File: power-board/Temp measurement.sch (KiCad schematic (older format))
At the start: 8 parts, among them U5 AT30TS74-XM

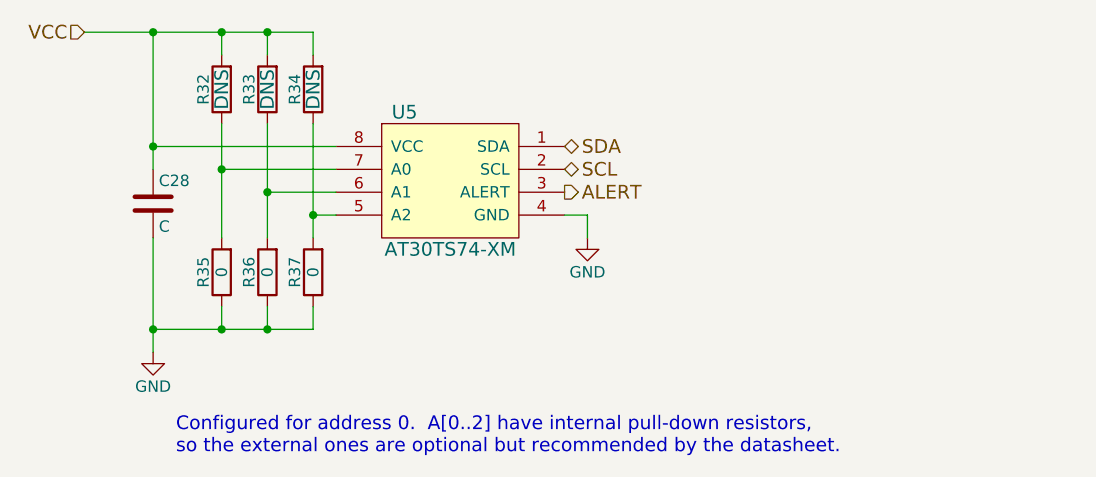
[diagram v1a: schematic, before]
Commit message: switched to XMEGA A4U
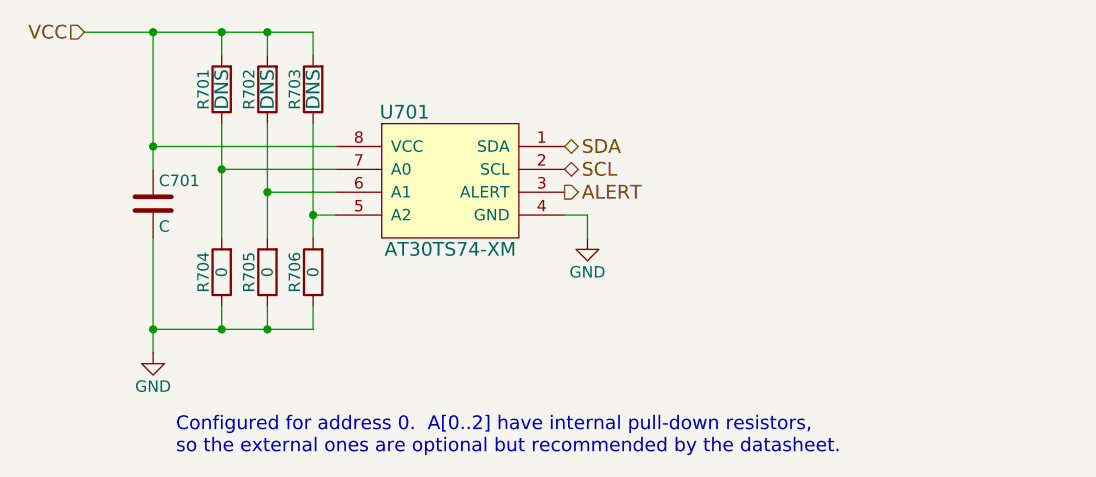
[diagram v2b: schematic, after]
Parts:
- renumbered C28 to C701, R32 to R701, R33 to R702, R34 to R703, R35 to R704, R36 to R705, R37 to R706, U5 to U701
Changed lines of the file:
@@
 $Descr A4 11693 8268
 encoding utf-8
-Sheet 7 10
+Sheet 7 11
 Title ""
 Date ""
@@
 $EndDescr
 $Comp
-L AT30TS74-XM U5
+L AT30TS74-XM U701
 U 1 1 59359173
 P 5500 3650
-F 0 "U5" H 5600 3700 60  0000 C CNN
+F 0 "U701" H 5600 3700 60  0000 C CNN
 F 1 "AT30TS74-XM" H 5800 3100 60  0000 C CNN
 F 2 "" H 5500 3650 60  0000 C CNN
@@
 ALERT
 $Comp
-L GND #PWR34
+L GND #PWR042
 U 1 1 5935935B
 P 6400 4150
-F 0 "#PWR34" H 6400 3900 50  0001 C CNN
+F 0 "#PWR042" H 6400 3900 50  0001 C CNN
 F 1 "GND" H 6400 4000 50  0000 C CNN
 F 2 "" H 6400 4150 50  0000 C CNN
@@
 	6400 4050 6400 4150
 $Comp
-L C C28
+L C C701
 U 1 1 59359380
 P 4500 4000
-F 0 "C28" H 4525 4100 50  0000 L CNN
+F 0 "C701" H 4525 4100 50  0000 L CNN
 F 1 "C" H 4525 3900 50  0000 L CNN
 F 2 "" H 4538 3850 50  0000 C CNN
@@
 $EndComp
 $Comp
-L R R37
+L R R706
 U 1 1 593595A6
 P 5200 4300
-F 0 "R37" V 5280 4300 50  0000 C CNN
+F 0 "R706" V 5280 4300 50  0000 C CNN
 F 1 "0" V 5200 4300 50  0000 C CNN
 F 2 "" V 5130 4300 50  0000 C CNN
@@
 $EndComp
 $Comp
-L R R36
+L R R705
 U 1 1 59359612
 P 5000 4300
-F 0 "R36" V 5080 4300 50  0000 C CNN
+F 0 "R705" V 5080 4300 50  0000 C CNN
 F 1 "0" V 5000 4300 50  0000 C CNN
 F 2 "" V 4930 4300 50  0000 C CNN
@@
 $EndComp
 $Comp
-L R R35
+L R R704
 U 1 1 59359639
 P 4800 4300
-F 0 "R35" V 4880 4300 50  0000 C CNN
+F 0 "R704" V 4880 4300 50  0000 C CNN
 F 1 "0" V 4800 4300 50  0000 C CNN
 F 2 "" V 4730 4300 50  0000 C CNN
@@
 $EndComp
 $Comp
-L R R32
+L R R701
 U 1 1 593597EF
 P 4800 3500
-F 0 "R32" V 4880 3500 50  0000 C CNN
+F 0 "R701" V 4880 3500 50  0000 C CNN
 F 1 "R" V 4800 3500 50  0001 C CNN
 F 2 "" V 4730 3500 50  0000 C CNN
@@
 	5000 4550 5000 4450
 $Comp
-L GND #PWR35
+L GND #PWR043
 U 1 1 59359C4C
 P 4500 4650
-F 0 "#PWR35" H 4500 4400 50  0001 C CNN
+F 0 "#PWR043" H 4500 4400 50  0001 C CNN
 F 1 "GND" H 4500 4500 50  0000 C CNN
 F 2 "" H 4500 4650 50  0000 C CNN
@@
 $EndComp
 $Comp
-L R R33
+L R R702
 U 1 1 59359E6E
 P 5000 3500
-F 0 "R33" V 5080 3500 50  0000 C CNN
+F 0 "R702" V 5080 3500 50  0000 C CNN
 F 1 "R" V 5000 3500 50  0001 C CNN
 F 2 "" V 4930 3500 50  0000 C CNN
@@
 $EndComp
 $Comp
-L R R34
+L R R703
 U 1 1 59359E9C
 P 5200 3500
-F 0 "R34" V 5280 3500 50  0000 C CNN
+F 0 "R703" V 5280 3500 50  0000 C CNN
 F 1 "R" V 5200 3500 50  0001 C CNN
 F 2 "" V 5130 3500 50  0000 C CNN

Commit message: routed board
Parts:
- C701: value C -> 0.1u; footprint (none) -> Capacitors_SMD:C_0603
- R701, R702, R703, R704, R705, R706: footprint (none) -> Resistors_SMD:R_0603
- U701: value AT30TS74-XM -> Main Reg; footprint (none) -> Housings_SSOP:MSOP-8_3x3mm_Pitch0.65mm
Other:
- moved on the sheet: R701, R702, R703, R704, R705, R706, U701
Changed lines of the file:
@@
 $Descr A4 11693 8268
 encoding utf-8
-Sheet 7 11
+Sheet 6 12
 Title ""
 Date ""
@@
 L AT30TS74-XM U701
 U 1 1 59359173
-P 5500 3650
-F 0 "U701" H 5600 3700 60  0000 C CNN
-F 1 "AT30TS74-XM" H 5800 3100 60  0000 C CNN
-F 2 "" H 5500 3650 60  0000 C CNN
-F 3 "" H 5500 3650 60  0000 C CNN
-F 4 "Microchip Technology" H 5500 3650 60  0001 C CNN "MFG"
-F 5 "AT30TS74-XM8M-B" H 5500 3650 60  0001 C CNN "MPN"
-	1    5500 3650
+P 6300 3700
+F 0 "U701" H 6400 3750 60  0000 C CNN
+F 1 "Main Reg" H 6600 3150 60  0000 C CNN
+F 2 "Housings_SSOP:MSOP-8_3x3mm_Pitch0.65mm" H 6300 3700 60  0001 C CNN
+F 3 "" H 6300 3700 60  0000 C CNN
+F 4 "Microchip Technology" H 6300 3700 60  0001 C CNN "MFG"
+F 5 "AT30TS74-XM8M-B" H 6300 3700 60  0001 C CNN "MPN"
+	1    6300 3700
 	1    0    0    -1
 $EndComp
-Text HLabel 4200 3250 0    60   Input ~ 0
+Text HLabel 5000 3300 0    60   Input ~ 0
 VCC
-Text HLabel 6300 3750 2    60   BiDi ~ 0
+Text HLabel 7100 3800 2    60   BiDi ~ 0
 SDA
-Text HLabel 6300 3850 2    60   BiDi ~ 0
+Text HLabel 7100 3900 2    60   BiDi ~ 0
 SCL
-Text HLabel 6300 3950 2    60   Output ~ 0
+Text HLabel 7100 4000 2    60   Output ~ 0
 ALERT
 $Comp
-L GND #PWR042
+L GND #PWR028
 U 1 1 5935935B
-P 6400 4150
-F 0 "#PWR042" H 6400 3900 50  0001 C CNN
-F 1 "GND" H 6400 4000 50  0000 C CNN
-F 2 "" H 6400 4150 50  0000 C CNN
-F 3 "" H 6400 4150 50  0000 C CNN
-	1    6400 4150
+P 7200 4200
+F 0 "#PWR028" H 7200 3950 50  0001 C CNN
+F 1 "GND" H 7200 4050 50  0000 C CNN
+F 2 "" H 7200 4200 50  0000 C CNN
+F 3 "" H 7200 4200 50  0000 C CNN
+	1    7200 4200
 	1    0    0    -1
 $EndComp
 Wire Wire Line
-	6300 4050 6400 4050
+	7100 4100 7200 4100
 Wire Wire Line
-	6400 4050 6400 4150
-$Comp
-L C C701
-U 1 1 59359380
-P 4500 4000
-F 0 "C701" H 4525 4100 50  0000 L CNN
-F 1 "C" H 4525 3900 50  0000 L CNN
-F 2 "" H 4538 3850 50  0000 C CNN
-F 3 "" H 4500 4000 50  0000 C CNN
-F 4 "Murata Electronics" H 4500 4000 60  0001 C CNN "MFG"
-F 5 "GRM188R71H104KA93D" H 4500 4000 60  0001 C CNN "MPN"
-	1    4500 4000
-	1    0    0    -1
-$EndComp
+	7200 4100 7200 4200
 $Comp
 L R R706
 U 1 1 593595A6
-P 5200 4300
-F 0 "R706" V 5280 4300 50  0000 C CNN
-F 1 "0" V 5200 4300 50  0000 C CNN
-F 2 "" V 5130 4300 50  0000 C CNN
-F 3 "" H 5200 4300 50  0000 C CNN
-	1    5200 4300
+P 6000 4350
+F 0 "R706" V 6080 4350 50  0000 C CNN
+F 1 "0" V 6000 4350 50  0000 C CNN
+F 2 "Resistors_SMD:R_0603" V 5930 4350 50  0001 C CNN
+F 3 "" H 6000 4350 50  0000 C CNN
+	1    6000 4350
 	-1   0    0    1
 $EndComp
@@
 L R R705
 U 1 1 59359612
-P 5000 4300
-F 0 "R705" V 5080 4300 50  0000 C CNN
-F 1 "0" V 5000 4300 50  0000 C CNN
-F 2 "" V 4930 4300 50  0000 C CNN
-F 3 "" H 5000 4300 50  0000 C CNN
-	1    5000 4300
+P 5800 4350
+F 0 "R705" V 5880 4350 50  0000 C CNN
+F 1 "0" V 5800 4350 50  0000 C CNN
+F 2 "Resistors_SMD:R_0603" V 5730 4350 50  0001 C CNN
+F 3 "" H 5800 4350 50  0000 C CNN
+	1    5800 4350
 	-1   0    0    1
 $EndComp
@@
 L R R704
 U 1 1 59359639
-P 4800 4300
-F 0 "R704" V 4880 4300 50  0000 C CNN
-F 1 "0" V 4800 4300 50  0000 C CNN
-F 2 "" V 4730 4300 50  0000 C CNN
-F 3 "" H 4800 4300 50  0000 C CNN
-	1    4800 4300
+P 5600 4350
+F 0 "R704" V 5680 4350 50  0000 C CNN
+F 1 "0" V 5600 4350 50  0000 C CNN
+F 2 "Resistors_SMD:R_0603" V 5530 4350 50  0001 C CNN
+F 3 "" H 5600 4350 50  0000 C CNN
+	1    5600 4350
 	-1   0    0    1
 $EndComp
@@
 L R R701
 U 1 1 593597EF
-P 4800 3500
-F 0 "R701" V 4880 3500 50  0000 C CNN
-F 1 "R" V 4800 3500 50  0001 C CNN
-F 2 "" V 4730 3500 50  0000 C CNN
-F 3 "" H 4800 3500 50  0000 C CNN
-F 4 "DNS" V 4800 3500 60  0000 C CNN "Note"
-	1    4800 3500
+P 5600 3550
+F 0 "R701" V 5680 3550 50  0000 C CNN
+F 1 "R" V 5600 3550 50  0001 C CNN
+F 2 "Resistors_SMD:R_0603" V 5530 3550 50  0001 C CNN
+F 3 "" H 5600 3550 50  0000 C CNN
+F 4 "DNS" V 5600 3550 60  0000 C CNN "Note"
+	1    5600 3550
 	-1   0    0    1
 $EndComp
 Wire Wire Line
-	5300 3850 4800 3850
+	6100 3900 5600 3900
 Wire Wire Line
-	4800 3650 4800 4150
-Connection ~ 4800 3850
+	5600 3700 5600 4200
+Connection ~ 5600 3900
 Wire Wire Line
-	5300 3950 5000 3950
+	6100 4000 5800 4000
 Wire Wire Line
-	5000 3650 5000 4150
-Connection ~ 5000 3950
+	5800 3700 5800 4200
+Connection ~ 5800 4000
 Wire Wire Line
-	5300 4050 5200 4050
+	6100 4100 6000 4100
 Wire Wire Line
-	5200 3650 5200 4150
-Connection ~ 5200 4050
+	6000 3700 6000 4200
+Connection ~ 6000 4100
 Wire Wire Line
-	5200 4550 5200 4450
+	6000 4600 6000 4500
 Wire Wire Line
-	4500 4550 5200 4550
+	5300 4600 6000 4600
 Wire Wire Line
-	4800 4550 4800 4450
-Connection ~ 5000 4550
+	5600 4600 5600 4500
+Connection ~ 5800 4600
 Wire Wire Line
-	4800 3250 4800 3350
+	5600 3300 5600 3400
 Wire Wire Line
-	4200 3250 5200 3250
+	5000 3300 6000 3300
 Wire Wire Line
-	5200 3250 5200 3350
+	6000 3300 6000 3400
 Wire Wire Line
-	5000 3350 5000 3250
-Connection ~ 5000 3250
-Connection ~ 4800 3250
+	5800 3400 5800 3300
+Connection ~ 5800 3300
+Connection ~ 5600 3300
 Wire Wire Line
-	5300 3750 4500 3750
+	6100 3800 5300 3800
 Wire Wire Line
-	4500 3250 4500 3850
-Connection ~ 4500 3250
-Connection ~ 4500 3750
+	5300 3300 5300 3900
+Connection ~ 5300 3300
+Connection ~ 5300 3800
 Wire Wire Line
-	4500 4150 4500 4650
-Connection ~ 4800 4550
-Connection ~ 4500 4550
+	5300 4200 5300 4700
+Connection ~ 5600 4600
+Connection ~ 5300 4600
 Wire Wire Line
-	5000 4550 5000 4450
+	5800 4600 5800 4500
 $Comp
-L GND #PWR043
+L GND #PWR029
 U 1 1 59359C4C
-P 4500 4650
-F 0 "#PWR043" H 4500 4400 50  0001 C CNN
-F 1 "GND" H 4500 4500 50  0000 C CNN
-F 2 "" H 4500 4650 50  0000 C CNN
-F 3 "" H 4500 4650 50  0000 C CNN
-	1    4500 4650
+P 5300 4700
+F 0 "#PWR029" H 5300 4450 50  0001 C CNN
+F 1 "GND" H 5300 4550 50  0000 C CNN
+F 2 "" H 5300 4700 50  0000 C CNN
+F 3 "" H 5300 4700 50  0000 C CNN
+	1    5300 4700
 	1    0    0    -1
 $EndComp
@@
 L R R702
 U 1 1 59359E6E
-P 5000 3500
-F 0 "R702" V 5080 3500 50  0000 C CNN
-F 1 "R" V 5000 3500 50  0001 C CNN
-F 2 "" V 4930 3500 50  0000 C CNN
-F 3 "" H 5000 3500 50  0000 C CNN
-F 4 "DNS" V 5000 3500 60  0000 C CNN "Note"
-	1    5000 3500
+P 5800 3550
+F 0 "R702" V 5880 3550 50  0000 C CNN
+F 1 "R" V 5800 3550 50  0001 C CNN
+F 2 "Resistors_SMD:R_0603" V 5730 3550 50  0001 C CNN
+F 3 "" H 5800 3550 50  0000 C CNN
+F 4 "DNS" V 5800 3550 60  0000 C CNN "Note"
+	1    5800 3550
 	-1   0    0    1
 $EndComp
@@
 L R R703
 U 1 1 59359E9C
-P 5200 3500
-F 0 "R703" V 5280 3500 50  0000 C CNN
-F 1 "R" V 5200 3500 50  0001 C CNN
-F 2 "" V 5130 3500 50  0000 C CNN
-F 3 "" H 5200 3500 50  0000 C CNN
-F 4 "DNS" V 5200 3500 60  0000 C CNN "Note"
-	1    5200 3500
+P 6000 3550
+F 0 "R703" V 6080 3550 50  0000 C CNN
+F 1 "R" V 6000 3550 50  0001 C CNN
+F 2 "Resistors_SMD:R_0603" V 5930 3550 50  0001 C CNN
+F 3 "" H 6000 3550 50  0000 C CNN
+F 4 "DNS" V 6000 3550 60  0000 C CNN "Note"
+	1    6000 3550
 	-1   0    0    1
 $EndComp
 Text Notes 4600 5100 0    60   ~ 0
 Configured for address 0.  A[0..2] have internal pull-down resistors,\nso the external ones are optional but recommended by the datasheet.
+$Comp
+L C C701
+U 1 1 593E171E
+P 5300 4050
+F 0 "C701" H 5325 4150 50  0000 L CNN
+F 1 "0.1u" H 5325 3950 50  0000 L CNN
+F 2 "Capacitors_SMD:C_0603" H 5338 3900 50  0001 C CNN
+F 3 "" H 5300 4050 50  0000 C CNN
+F 4 "Murata Electronics" H 5300 4050 60  0001 C CNN "MFG"
+F 5 "GRM188R71H104KA93D" H 5300 4050 60  0001 C CNN "MPN"
+	1    5300 4050
+	1    0    0    -1
+$EndComp
 $EndSCHEMATC

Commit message: adding more part numbers
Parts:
- R701, R702, R703, R704, R705, R706: MFG (none) -> Yageo; MPN (none) -> RC0603JR-070RL
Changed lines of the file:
@@
 	7200 4100 7200 4200
-$Comp
-L R R706
-U 1 1 593595A6
-P 6000 4350
-F 0 "R706" V 6080 4350 50  0000 C CNN
-F 1 "0" V 6000 4350 50  0000 C CNN
-F 2 "Resistors_SMD:R_0603" V 5930 4350 50  0001 C CNN
-F 3 "" H 6000 4350 50  0000 C CNN
-	1    6000 4350
-	-1   0    0    1
-$EndComp
-$Comp
-L R R705
-U 1 1 59359612
-P 5800 4350
-F 0 "R705" V 5880 4350 50  0000 C CNN
-F 1 "0" V 5800 4350 50  0000 C CNN
-F 2 "Resistors_SMD:R_0603" V 5730 4350 50  0001 C CNN
-F 3 "" H 5800 4350 50  0000 C CNN
-	1    5800 4350
-	-1   0    0    1
-$EndComp
 $Comp
 L R R704
@@
 F 2 "Resistors_SMD:R_0603" V 5530 4350 50  0001 C CNN
 F 3 "" H 5600 4350 50  0000 C CNN
+F 4 "Yageo" V 5600 4350 60  0001 C CNN "MFG"
+F 5 "RC0603JR-070RL" V 5600 4350 60  0001 C CNN "MPN"
 	1    5600 4350
 	-1   0    0    1
@@
 F 3 "" H 5600 3550 50  0000 C CNN
 F 4 "DNS" V 5600 3550 60  0000 C CNN "Note"
+F 5 "Yageo" V 5600 3550 60  0001 C CNN "MFG"
+F 6 "RC0603JR-070RL" V 5600 3550 60  0001 C CNN "MPN"
 	1    5600 3550
 	-1   0    0    1
@@
 	1    0    0    -1
 $EndComp
-$Comp
-L R R702
-U 1 1 59359E6E
-P 5800 3550
-F 0 "R702" V 5880 3550 50  0000 C CNN
-F 1 "R" V 5800 3550 50  0001 C CNN
-F 2 "Resistors_SMD:R_0603" V 5730 3550 50  0001 C CNN
-F 3 "" H 5800 3550 50  0000 C CNN
-F 4 "DNS" V 5800 3550 60  0000 C CNN "Note"
-	1    5800 3550
-	-1   0    0    1
-$EndComp
-$Comp
-L R R703
-U 1 1 59359E9C
-P 6000 3550
-F 0 "R703" V 6080 3550 50  0000 C CNN
-F 1 "R" V 6000 3550 50  0001 C CNN
-F 2 "Resistors_SMD:R_0603" V 5930 3550 50  0001 C CNN
-F 3 "" H 6000 3550 50  0000 C CNN
-F 4 "DNS" V 6000 3550 60  0000 C CNN "Note"
-	1    6000 3550
-	-1   0    0    1
-$EndComp
 Text Notes 4600 5100 0    60   ~ 0
 Configured for address 0.  A[0..2] have internal pull-down resistors,\nso the external ones are optional but recommended by the datasheet.
@@
 	1    0    0    -1
 $EndComp
+$Comp
+L R R705
+U 1 1 59AB8DA0
+P 5800 4350
+F 0 "R705" V 5880 4350 50  0000 C CNN
+F 1 "0" V 5800 4350 50  0000 C CNN
+F 2 "Resistors_SMD:R_0603" V 5730 4350 50  0001 C CNN
+F 3 "" H 5800 4350 50  0000 C CNN
+F 4 "Yageo" V 5800 4350 60  0001 C CNN "MFG"
+F 5 "RC0603JR-070RL" V 5800 4350 60  0001 C CNN "MPN"
+	1    5800 4350
+	-1   0    0    1
+$EndComp
+$Comp
+L R R706
+U 1 1 59AB8DCD
+P 6000 4350
+F 0 "R706" V 6080 4350 50  0000 C CNN
+F 1 "0" V 6000 4350 50  0000 C CNN
+F 2 "Resistors_SMD:R_0603" V 5930 4350 50  0001 C CNN
+F 3 "" H 6000 4350 50  0000 C CNN
+F 4 "Yageo" V 6000 4350 60  0001 C CNN "MFG"
+F 5 "RC0603JR-070RL" V 6000 4350 60  0001 C CNN "MPN"
+	1    6000 4350
+	-1   0    0    1
+$EndComp
+$Comp
+L R R702
+U 1 1 59ABAD46
+P 5800 3550
+F 0 "R702" V 5880 3550 50  0000 C CNN
+F 1 "R" V 5800 3550 50  0001 C CNN
+F 2 "Resistors_SMD:R_0603" V 5730 3550 50  0001 C CNN
+F 3 "" H 5800 3550 50  0000 C CNN
+F 4 "DNS" V 5800 3550 60  0000 C CNN "Note"
+F 5 "Yageo" V 5800 3550 60  0001 C CNN "MFG"
+F 6 "RC0603JR-070RL" V 5800 3550 60  0001 C CNN "MPN"
+	1    5800 3550
+	-1   0    0    1
+$EndComp
+$Comp
+L R R703
+U 1 1 59ABAD73
+P 6000 3550
+F 0 "R703" V 6080 3550 50  0000 C CNN
+F 1 "R" V 6000 3550 50  0001 C CNN
+F 2 "Resistors_SMD:R_0603" V 5930 3550 50  0001 C CNN
+F 3 "" H 6000 3550 50  0000 C CNN
+F 4 "DNS" V 6000 3550 60  0000 C CNN "Note"
+F 5 "Yageo" V 6000 3550 60  0001 C CNN "MFG"
+F 6 "RC0603JR-070RL" V 6000 3550 60  0001 C CNN "MPN"
+	1    6000 3550
+	-1   0    0    1
+$EndComp
 $EndSCHEMATC
